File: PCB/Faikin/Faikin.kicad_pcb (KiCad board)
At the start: 2 copper layers, 70 x 70 mm, 27 parts, among them J1 1x5, J3 USB-PROG, Q1 BSS138PS, U3 MD8942, U4 ESP32-S3-MINI-1

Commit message: Slightly rearranged
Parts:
- moved J3 0.85 mm to (137.9, 65.0)
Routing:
- net GND: track 21.3 -> 16.1 mm
- net +3.3V: track 38.2 -> 39.3 mm
- net DC: track 17.7 -> 18.5 mm
- net D+: track 4.63 -> 5.48 mm
- net D-: track 4.97 -> 5.71 mm

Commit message: Tidy USB even more
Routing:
- net D-: track 5.71 -> 3.07 mm
- net GND: track 16.1 -> 13.5 mm
- net DC: track 18.5 -> 16.1 mm
- net D+: track 5.48 -> 3.01 mm
- net +3.3V: track 39.3 -> 38.1 mm

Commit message: TC2030
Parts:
- removed J3: USB-PROG, RevK:USB-PROG2
- added J2: Conn_01x06, RevK:Tag-Connect_TC2030-IDC-NL_2x03_P1.27mm_Vertical, B.Cu at (138.7, 65.3)
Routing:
- net DC: track 16.1 -> 17.5 mm
- net D-: track 3.07 -> 2.72 mm, vias 0 -> 1
- net D+: track 3.01 -> 2.68 mm, vias 0 -> 1
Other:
- board text added: "B"

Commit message: TC2030-USB-NL cable pin out
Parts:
- removed J2: Conn_01x06, RevK:Tag-Connect_TC2030-IDC-NL_2x03_P1.27mm_Vertical
- added J3: TC2030-USB-NL, RevK:Tag-Connect_TC2030-IDC-NL_2x03_P1.27mm_Vertical, B.Cu at (139.4, 65.0)
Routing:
- net D+: track 2.68 -> 6.09 mm
- net DC: track 17.5 -> 19.7 mm
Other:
- board text added: "U"

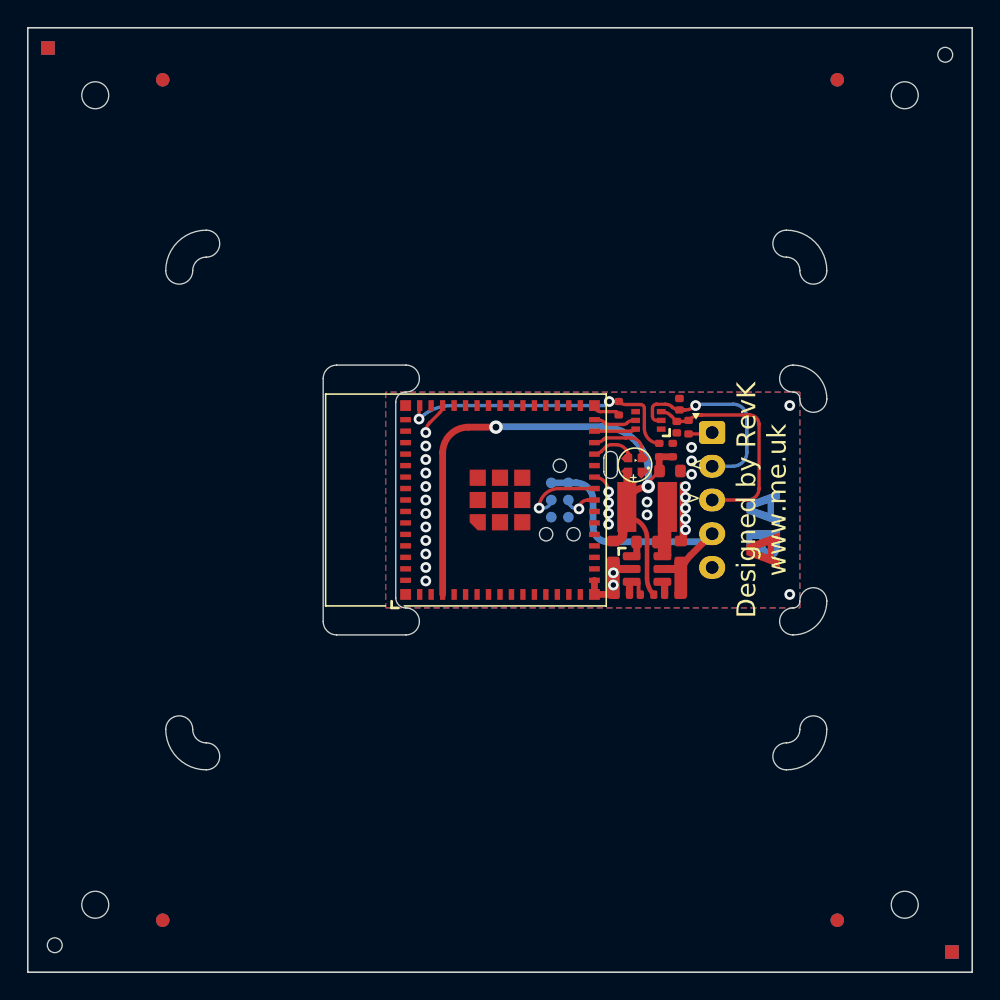
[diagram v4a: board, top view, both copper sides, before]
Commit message: Reworked for TC2030-USB-NL
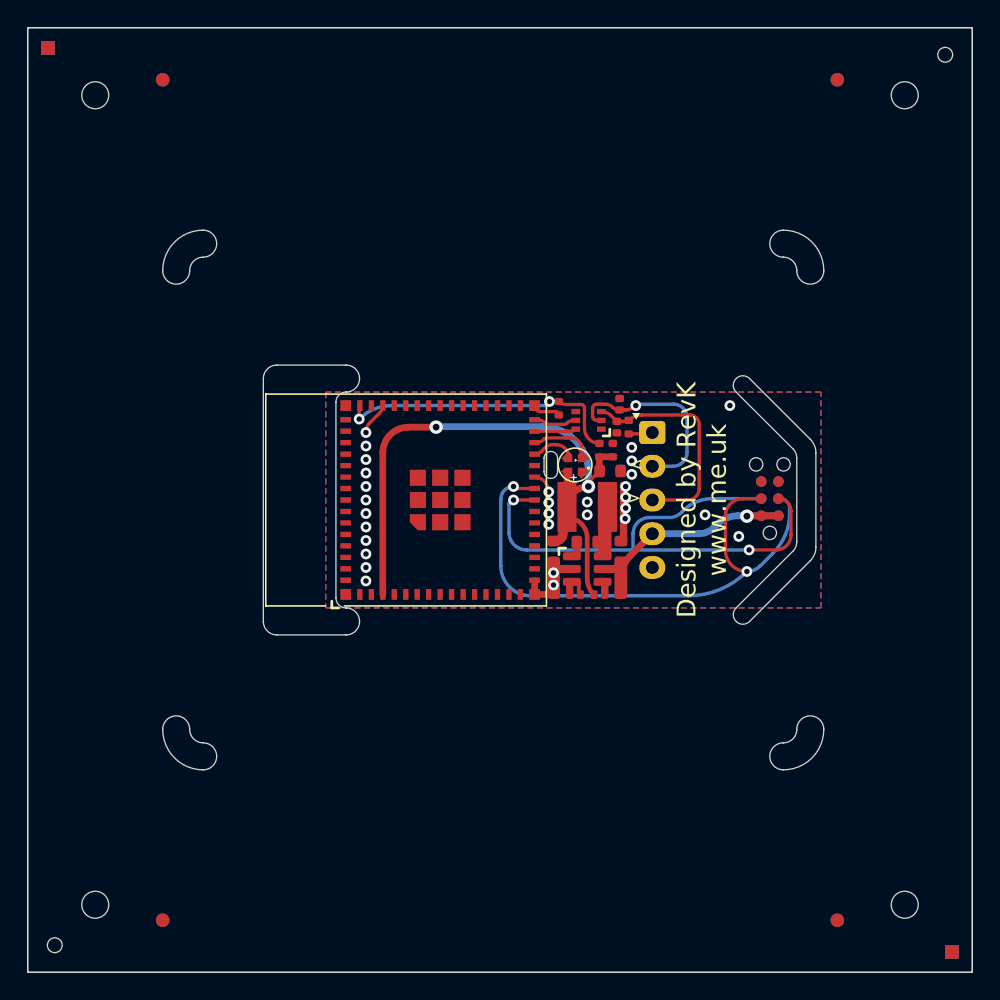
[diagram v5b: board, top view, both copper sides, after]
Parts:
- removed J3: TC2030-USB-NL, RevK:Tag-Connect_TC2030-IDC-NL_2x03_P1.27mm_Vertical
- added J2: TC2030-USB-NL-DS, RevK:Tag-Connect_TC2030-IDC-NL_2x03_P1.27mm_Vertical_DoubleSided, F.Cu at (155.0, 64.9)
- moved C10 4.44 mm to (141.5, 68.1)
- moved C2 4.44 mm to (143.4, 61.3)
- moved C5 4.44 mm to (143.2, 62.9)
- moved C6 4.44 mm to (139.4, 58.2)
- moved C8 4.44 mm to (144.0, 68.8)
- moved C9 4.44 mm to (139.0, 68.8)
- moved D1 4.44 mm to (140.6, 62.4)
- moved D2 4.44 mm to (143.7, 59.6)
- moved D3 4.44 mm to (143.9, 57.9)
- moved J1 4.44 mm to (146.3, 60.0)
- moved L2 4.44 mm to (141.5, 65.5)
- moved Q1 4.44 mm to (141.6, 59.1)
- moved R1 4.44 mm to (144.5, 59.6)
- moved R10 4.44 mm to (139.7, 72.0)
- moved R11 4.44 mm to (143.3, 72.0)
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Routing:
- net D-: track 2.63 -> 41.2 mm, vias 1 -> 2
- net D+: track 6.09 -> 43.5 mm, vias 1 -> 2
- net DC: track 19.7 -> 16.2 mm, vias 0 -> 1
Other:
- board text removed: "AB"
- board text removed: "U"

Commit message: Tidy
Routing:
- net D+: track 43.5 -> 44.4 mm
- net GND: vias 30 -> 42

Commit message: Tweaked PCb
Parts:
- J2: footprint RevK:Tag-Connect_TC2030-IDC-NL_2x03_P1.27mm_Vertical_DoubleSided -> RevK:Tag-Connect_TC2030-IDC-NL_2x03_P1.27mm_Vertical; moved to B.Cu
- V6: moved to B.Cu
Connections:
- U4 pad 19: GND -> +3.3V
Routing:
- net +3.3V: track 38.1 -> 23.1 mm, vias 2 -> 0
- net D-: track 41.4 -> 28.0 mm, vias 2 -> 3
- net D+: track 44.4 -> 35.4 mm
- net DC: track 16.5 -> 13.9 mm
- net GND: vias 42 -> 47
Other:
- board text added: "5"
- board text added: "U"

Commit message: Origin
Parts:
- moved C10 0.74 mm to (140.7, 68.1)
- moved C2 0.74 mm to (142.6, 61.3)
- moved C6 0.74 mm to (138.6, 58.2)
- moved C8 0.74 mm to (143.2, 68.8)
- moved C9 0.74 mm to (138.2, 68.8)
- moved D3 0.74 mm to (143.1, 57.9)
- moved L2 0.74 mm to (140.7, 65.5)
- moved R3 0.74 mm to (141.6, 61.3)
- moved R9 0.74 mm to (140.7, 72.0)
- moved U3 0.74 mm to (140.7, 70.1)
- moved C5 0.73 mm to (142.4, 62.9)
- moved D1 0.73 mm to (139.8, 62.4)
- moved D2 0.73 mm to (142.9, 59.6)
- moved J1 0.73 mm to (145.6, 60.0)
- moved Q1 0.73 mm to (140.8, 59.1)
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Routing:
- net D+: track 35.4 -> 36.1 mm
- net GND: vias 47 -> 48
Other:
- board text added: "®"
